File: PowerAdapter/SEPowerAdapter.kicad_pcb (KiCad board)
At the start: 2 copper layers, 48 x 94.6 mm, 34 parts, among them J1 XOR, J2 ATX, J3 Mac, J4 VGA, U1 LM7905_TO220, U2 74LVC86AD, U3 74LVC86AD

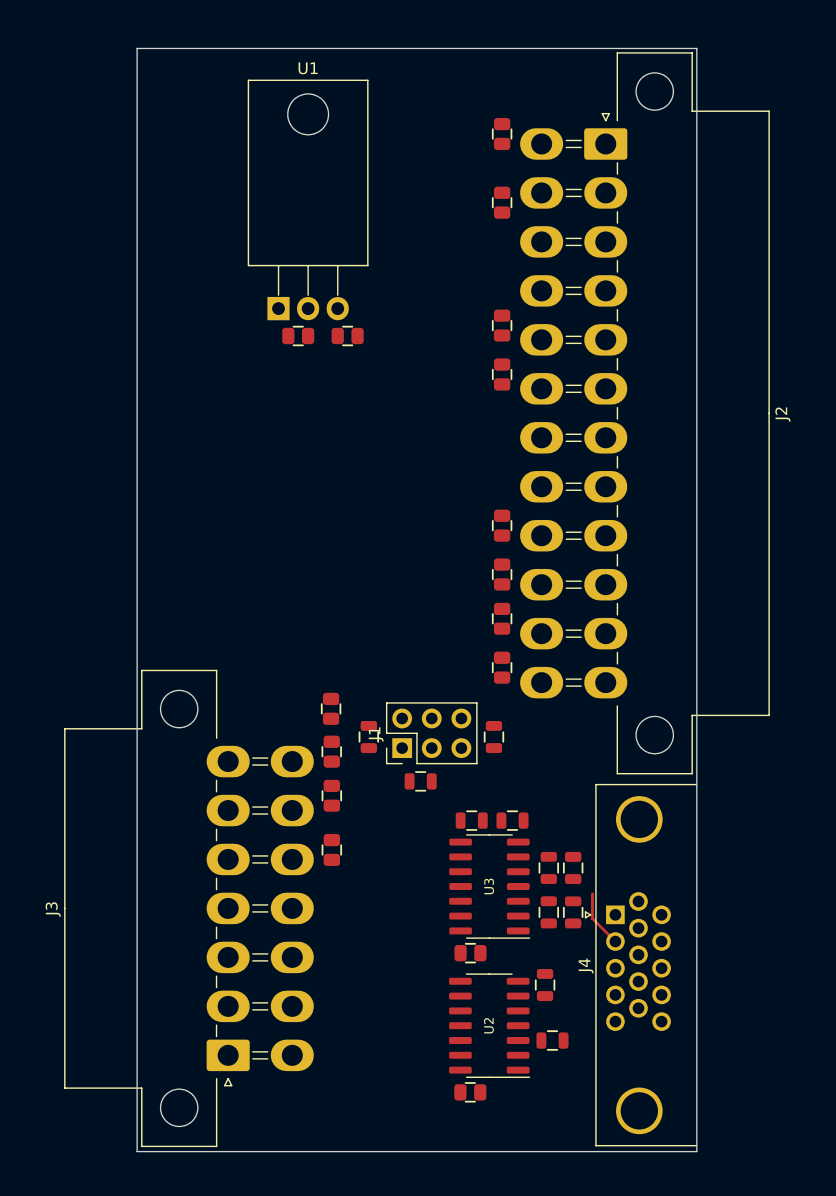
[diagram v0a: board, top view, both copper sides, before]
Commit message: Correct orientation for ROM sockets
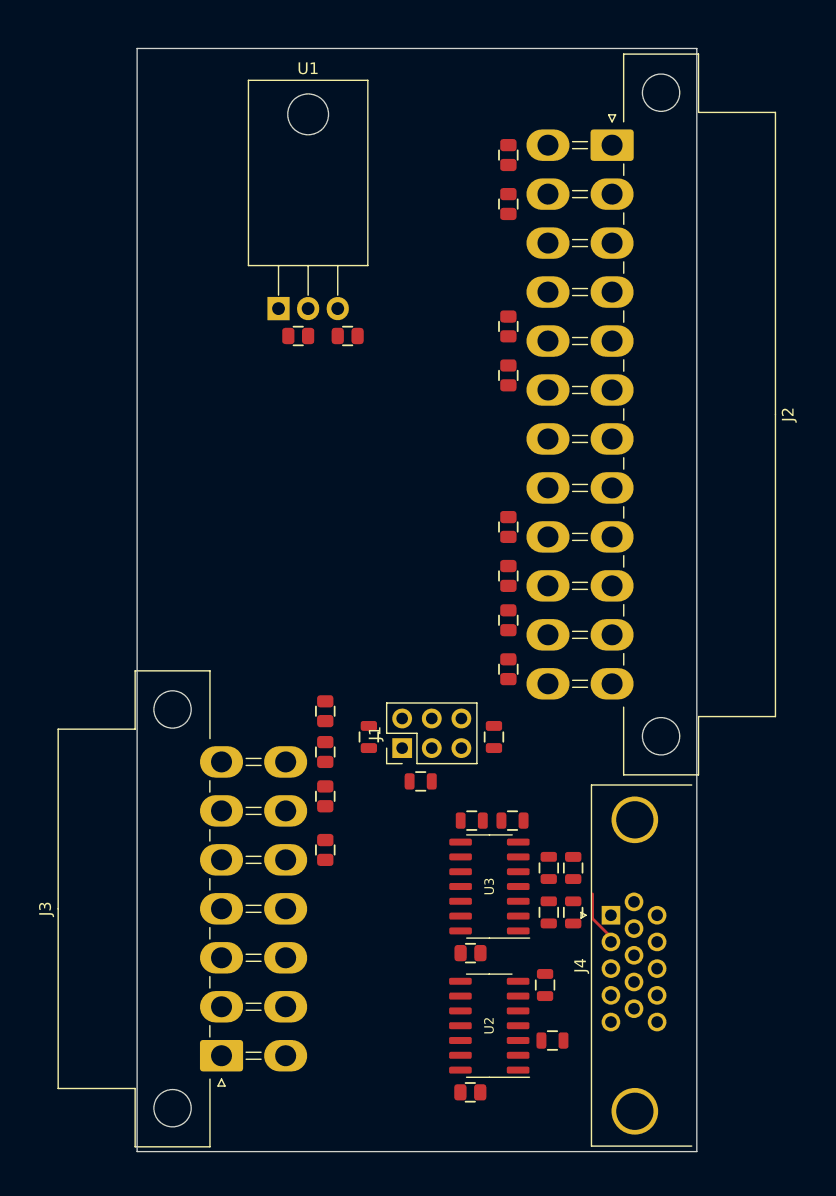
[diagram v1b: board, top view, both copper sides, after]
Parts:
- moved C9 1.88 mm to (109.5, 107.2), turned to -90 degrees
- moved J3 0.57 mm to (84.9, 184.5)
- moved C15 0.56 mm to (93.8, 162.2)
- moved C6 0.56 mm to (93.8, 166.8)
- moved J2 0.55 mm to (118.4, 106.4)
- moved C1 0.55 mm to (93.8, 158.4)
- moved C8 0.55 mm to (109.5, 151.3)
- moved C2 0.55 mm to (109.5, 147.2)
- moved C4 0.55 mm to (109.5, 143.3)
- moved C13 0.55 mm to (109.5, 111.5)
- moved C3 0.55 mm to (109.5, 139.2)
- moved C7 0.54 mm to (109.5, 126.2)
- moved C5 0.54 mm to (109.5, 122.0)
- moved C12 0.54 mm to (93.8, 154.9)
- moved J4 0.39 mm to (118.3, 172.4)
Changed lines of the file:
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@@
   )
   (footprint "stdpads:C_0805" (layer "F.Cu")
-    (at 108.966 147.0235 -90)
+    (at 109.5 147.15 -90)
     (tags "capacitor")
     (property "Sheetfile" "SEPowerAdapter.kicad_sch")
@@
   )
   (footprint "Connector_Molex:Molex_Mini-Fit_Jr_5569-14A1_2x07_P4.20mm_Horizontal" (layer "F.Cu")
-    (at 85.471 184.4675 90)
+    (at 84.9 184.5 90)
     (descr "Molex Mini-Fit Jr. Power Connectors, old mpn/engineering number: 5569-14A1, example for new mpn: 39-29-4149, 7 Pins per row, Mounting: PCB Mounting Flange (http://www.molex.com/pdm_docs/sd/039291047_sd.pdf), generated with kicad-footprint-generator")
     (tags "connector Molex Mini-Fit_Jr top entryscrew_flange")
@@
   )
   (footprint "stdpads:C_0805" (layer "F.Cu")
-    (at 108.966 126.0685 -90)
+    (at 109.5 126.15 -90)
     (tags "capacitor")
     (property "Sheetfile" "SEPowerAdapter.kicad_sch")
@@
   )
   (footprint "Connector_Molex:Molex_Mini-Fit_Jr_5569-24A1_2x12_P4.20mm_Horizontal" (layer "F.Cu")
-    (at 117.856 106.299 -90)
+    (at 118.4 106.4 -90)
     (descr "Molex Mini-Fit Jr. Power Connectors, old mpn/engineering number: 5569-24A1, example for new mpn: 39-29-4249, 12 Pins per row, Mounting: PCB Mounting Flange (http://www.molex.com/pdm_docs/sd/039291047_sd.pdf), generated with kicad-footprint-generator")
     (tags "connector Molex Mini-Fit_Jr top entryscrew_flange")
@@
   )
   (footprint "stdpads:C_0805" (layer "F.Cu")
-    (at 94.352 158.426 90)
+    (at 93.8 158.45 90)
     (tags "capacitor")
     (property "Sheetfile" "SEPowerAdapter.kicad_sch")
@@
   )
   (footprint "stdpads:C_0805" (layer "F.Cu")
-    (at 94.2975 154.7495 -90)
+    (at 93.8 154.949999 -90)
     (tags "capacitor")
     (property "Sheetfile" "SEPowerAdapter.kicad_sch")
@@
   )
   (footprint "stdpads:C_0805" (layer "F.Cu")
-    (at 108.966 143.228 90)
+    (at 109.5 143.35 90)
     (tags "capacitor")
     (property "Sheetfile" "SEPowerAdapter.kicad_sch")
@@
   )
   (footprint "stdpads:C_0805" (layer "F.Cu")
-    (at 94.361 162.2035 90)
+    (at 93.8 162.25 90)
     (tags "capacitor")
     (property "Sheetfile" "SEPowerAdapter.kicad_sch")
@@
   )
   (footprint "stdpads:C_0805" (layer "F.Cu")
-    (at 108.966 111.3365 90)
+    (at 109.5 111.45 90)
     (tags "capacitor")
     (property "Sheetfile" "SEPowerAdapter.kicad_sch")
@@
   )
   (footprint "Connector_Dsub:DSUB-15-HD_Female_Horizontal_P2.29x1.98mm_EdgePinOffset3.03mm_Housed_MountingHolesOffset4.94mm" (layer "F.Cu")
-    (at 118.685169 172.414499 90)
+    (at 118.299669 172.45 90)
     (descr "15-pin D-Sub connector, horizontal/angled (90 deg), THT-mount, female, pitch 2.29x1.98mm, pin-PCB-offset 3.0300000000000002mm, distance of mounting holes 25mm, distance of mounting holes to PCB edge 4.9399999999999995mm, see https://disti-assets.s3.amazonaws.com/tonar/files/datasheets/16730.pdf")
     (tags "15-pin D-Sub connector horizontal angled 90deg THT female pitch 2.29x1.98mm pin-PCB-offset 3.0300000000000002mm mounting-holes-distance 25mm mounting-hole-offset 25mm")
@@
   )
   (footprint "stdpads:C_0805" (layer "F.Cu")
-    (at 94.361 166.8535 90)
+    (at 93.8 166.85 90)
     (tags "capacitor")
     (property "Sheetfile" "SEPowerAdapter.kicad_sch")
@@
   )
   (footprint "stdpads:C_0805" (layer "F.Cu")
-    (at 108.966 105.4455 90)
+    (at 109.5 107.25 -90)
     (tags "capacitor")
     (property "Sheetfile" "SEPowerAdapter.kicad_sch")
@@
     (fp_line (start -1 -0.625) (end 1 -0.625) (layer "F.Fab") (width 0.15))
     (fp_line (start 1 0.625) (end -1 0.625) (layer "F.Fab") (width 0.15))
-    (pad "1" smd roundrect locked (at -0.85 0 90) (size 1.05 1.4) (layers "F.Cu" "F.Paste" "F.Mask") (roundrect_rratio 0.25)
+    (pad "1" smd roundrect locked (at -0.85 0 270) (size 1.05 1.4) (layers "F.Cu" "F.Paste" "F.Mask") (roundrect_rratio 0.25)
       (net 4 "+3V3") (pintype "passive"))
-    (pad "2" smd roundrect locked (at 0.85 0 90) (size 1.05 1.4) (layers "F.Cu" "F.Paste" "F.Mask") (roundrect_rratio 0.25)
+    (pad "2" smd roundrect locked (at 0.85 0 270) (size 1.05 1.4) (layers "F.Cu" "F.Paste" "F.Mask") (roundrect_rratio 0.25)
       (net 2 "GND") (pintype "passive"))
     (model "${KICAD6_3DMODEL_DIR}/Capacitor_SMD.3dshapes/C_0805_2012Metric.wrl"
@@
   )
   (footprint "stdpads:C_0805" (layer "F.Cu")
-    (at 108.966 121.8775 -90)
+    (at 109.5 121.95 -90)
     (tags "capacitor")
     (property "Sheetfile" "SEPowerAdapter.kicad_sch")
@@
   )
   (footprint "stdpads:C_0805" (layer "F.Cu")
-    (at 108.966 139.037 90)
+    (at 109.5 139.15 90)
     (tags "capacitor")
     (property "Sheetfile" "SEPowerAdapter.kicad_sch")
@@
   )
   (footprint "stdpads:C_0805" (layer "F.Cu")
-    (at 108.966 151.2145 -90)
-    (tags "capacitor")
-    (property "Sheetfile" "SEPowerAdapter.kicad_sch")
+    (at 109.5 151.35 -90)
+    (tags "capacitor")
+    (property "Sheetfile" "SEPowerAdapter.kicad_sch")

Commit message: Finished power adapter?
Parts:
- added REF**: , stdpads:PasteHole_1.152mm_NPTH, F.Cu at (80.3, 100.8)
- added REF**: , stdpads:PasteHole_1.152mm_NPTH, F.Cu at (83.4, 191.1)
- added REF**: , stdpads:PasteHole_1.152mm_NPTH, F.Cu at (119.6, 99.8)
- added REF**: , stdpads:PasteHole_1.152mm_NPTH, F.Cu at (124.0, 189.3)
- C1, C10, C11, C12, C13, C14, C15, C16, C2, C3, C4, C5, C6, C7, C8, C9: value 2u2 -> 10u
- J3: footprint Connector_Molex:Molex_Mini-Fit_Jr_5569-14A1_2x07_P4.20mm_Horizontal -> stdpads:Molex_Mini-Fit_Jr_5569-14A1_2x07_P4.20mm_Horizontal
- U1: footprint Package_TO_SOT_THT:TO-220-3_Horizontal_TabDown -> stdpads:TO-220-3_Horizontal_TabDown
- moved R3 33.3 mm to (92.3, 190.1), turned to -90 degrees
- moved J1 31.4 mm to (95.2, 189.1)
- moved R2 28.0 mm to (110.0, 187.8)
- moved U1 16.0 mm to (91.6, 136.3)
- moved C11 15.9 mm to (90.7, 138.7)
- moved C14 15.9 mm to (95.0, 138.7)
- moved R1 13.5 mm to (103.1, 169.7), turned to -90 degrees
- moved J3 12.6 mm to (84.9, 171.9)
- moved R5 1.39 mm to (113.3, 179.6), turned to 0 degrees
- moved R4 0.27 mm to (113.3, 183.5)
- moved U2 0.26 mm to (107.9, 182.2)
- moved C16 0.20 mm to (106.3, 187.8)
- moved R11 0.06 mm to (115.1, 172.2)
- moved R9 0.06 mm to (115.1, 168.4)
- moved R6 0.06 mm to (106.4, 164.3)
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- renumbered R6 to R10, R7 to R11, R10 to R6, R11 to R7
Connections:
- R10 pad 2: /Ro -> /Bo
- R11 pad 2: /Ro -> /Bo
- R6 pad 2: /Bo -> /Ro
- R7 pad 2: /Bo -> /Ro
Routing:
- net +3V3: track 0.00 -> 158.7 mm, vias 0 -> 7
- net +5V: track 0.00 -> 128.8 mm
- net GND: track 0.00 -> 94.0 mm, vias 0 -> 86
- net -12V: track 0.00 -> 85.8 mm
- net /Cx: track 0.00 -> 63.5 mm, vias 0 -> 2
- net +12V: track 0.00 -> 45.6 mm
- net -5V: track 0.00 -> 43.9 mm
- net /Ci: track 0.00 -> 42.5 mm, vias 0 -> 2
- net /VSx: track 0.00 -> 32.2 mm
- net /HSx: track 0.00 -> 28.2 mm
- net /VSi: track 0.00 -> 24.2 mm
- net /HSi: track 0.00 -> 24.1 mm
- net /HSo: track 0.00 -> 19.6 mm
- net /Ro: track 0.00 -> 19.5 mm
- net /VSo: track 0.00 -> 16.7 mm
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- added copper zone on F.Cu, net -12V
- added copper zone on B.Cu, net GND
- added copper zone on F.Cu, net GND
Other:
- outline, holes or cut-outs redrawn
